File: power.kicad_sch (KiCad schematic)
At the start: 47 parts, among them J5 Ride Through, Q3 2N7002, U2 MAX17614, U3 TVS3300DRV, U4 LM61480

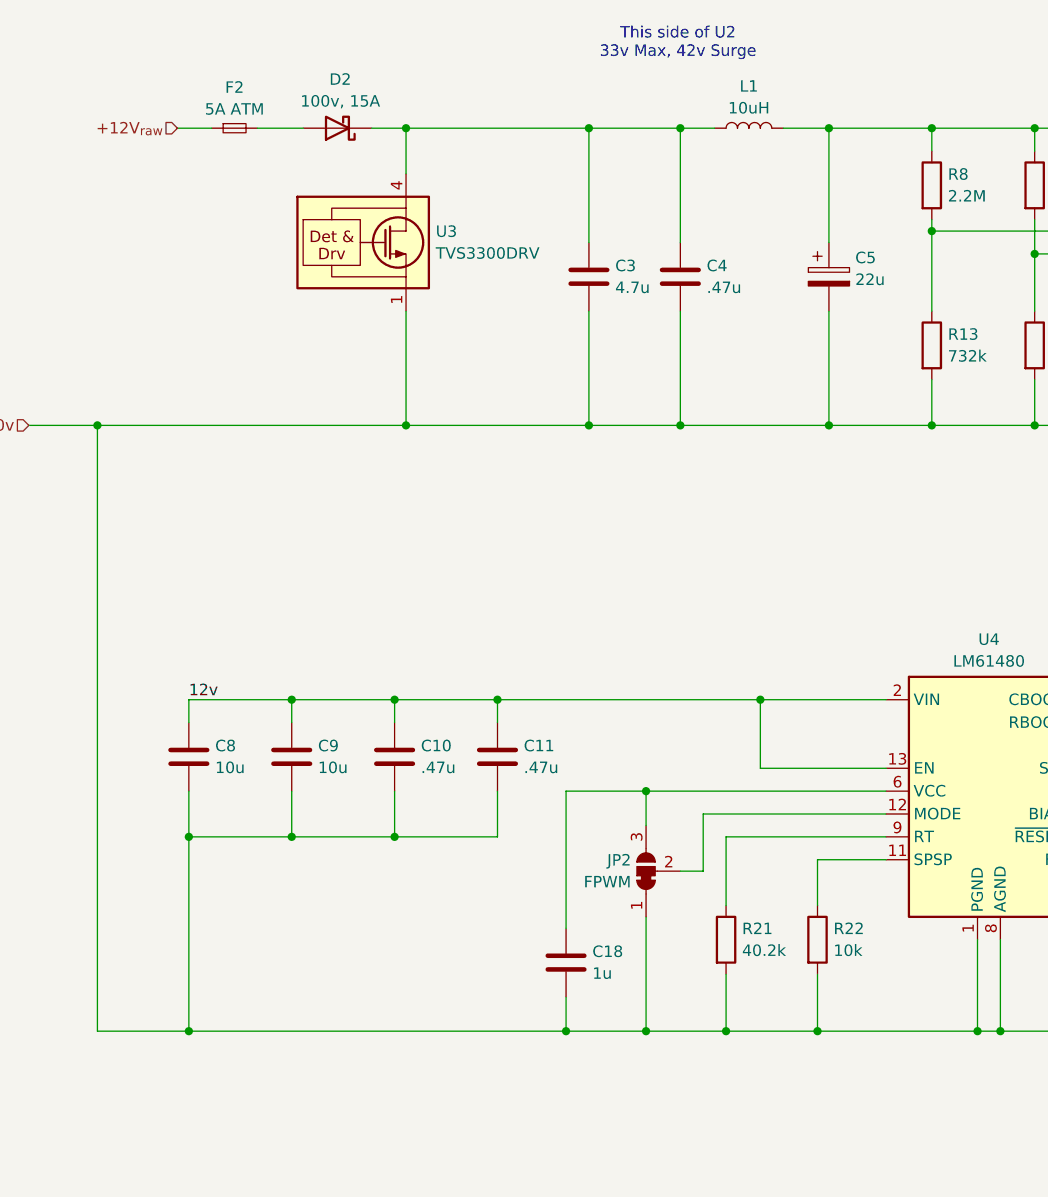
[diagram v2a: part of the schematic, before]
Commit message: second pass at layout complete
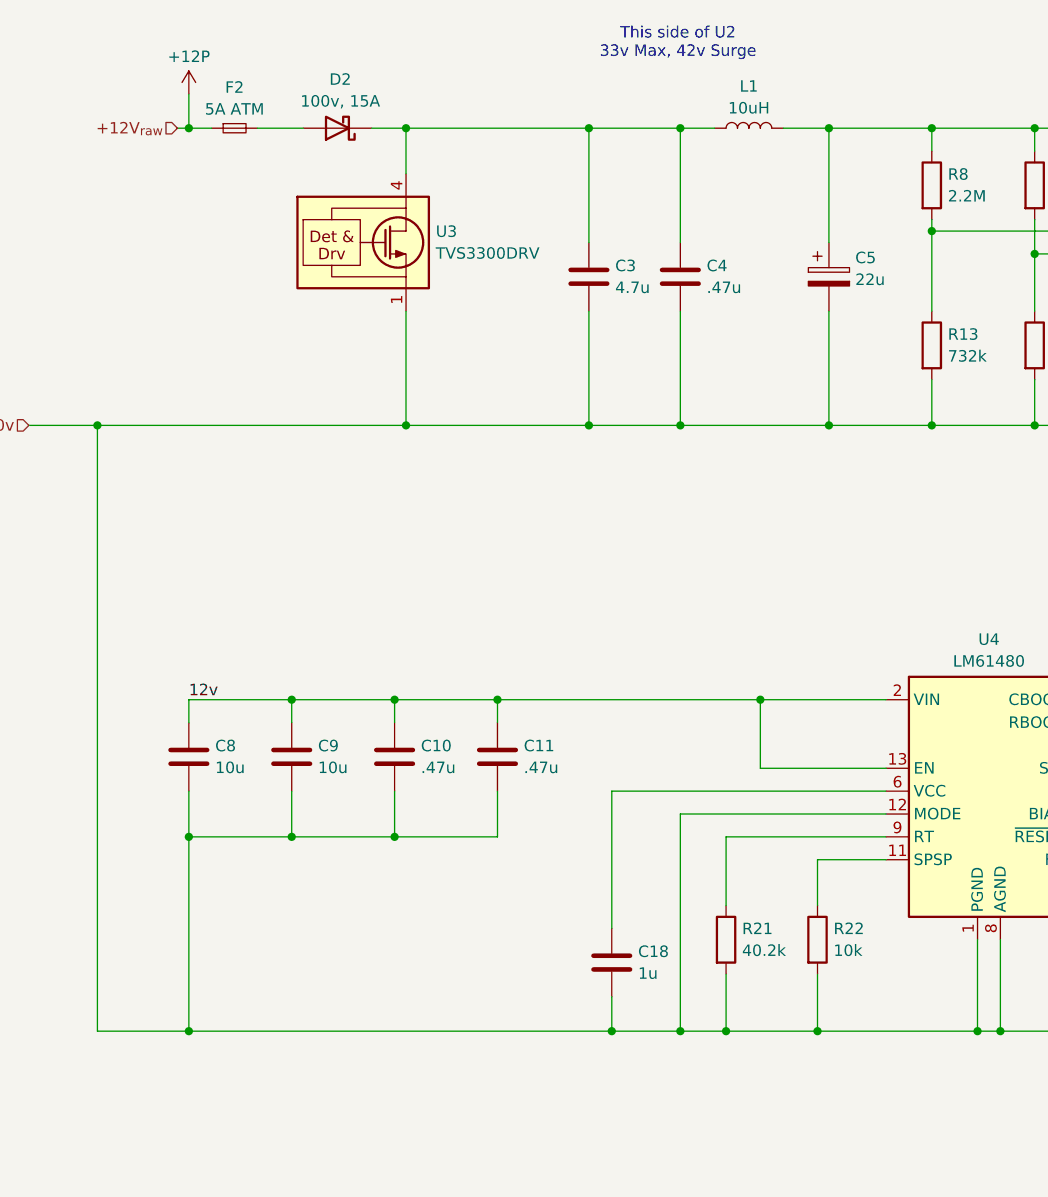
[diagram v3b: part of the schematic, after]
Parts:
- removed JP2: FPWM, Jumper:SolderJumper-3_P1.3mm_Bridged2Bar12_RoundedPad1.0x1.5mm, symbol Jumper:SolderJumper_3_Bridged12
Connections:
- net PGND: now also U4.12 (MODE)
- net +12V_{raw} renamed +12P
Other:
- moved on the sheet: C18
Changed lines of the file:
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@@
 	)
 	(junction
+		(at 85.09 133.35)
+		(diameter 0)
+		(color 0 0 0 0)
+	)
+	(junction
 		(at 260.35 33.02)
 		(diameter 0)
@@
 	)
 	(junction
+		(at 92.71 133.35)
+		(diameter 0)
+		(color 0 0 0 0)
+	)
+	(junction
 		(at 101.6 96.52)
 		(diameter 0)
@@
 	)
 	(junction
+		(at 38.1 33.02)
+		(diameter 0)
+		(color 0 0 0 0)
+	)
+	(junction
 		(at 60.96 111.76)
 		(diameter 0)
@@
 	)
 	(junction
-		(at 88.9 106.68)
-		(diameter 0)
-		(color 0 0 0 0)
-	)
-	(junction
 		(at 132.08 33.02)
 		(diameter 0)
@@
 	)
 	(junction
-		(at 88.9 133.35)
-		(diameter 0)
-		(color 0 0 0 0)
-	)
-	(junction
 		(at 227.33 33.02)
 		(diameter 0)
@@
 	)
 	(junction
-		(at 80.01 133.35)
-		(diameter 0)
-		(color 0 0 0 0)
-	)
-	(junction
 		(at 38.1 111.76)
 		(diameter 0)
@@
 	(wire
 		(pts
-			(xy 80.01 133.35) (xy 88.9 133.35)
-		)
-		(stroke
-			(width 0)
-			(type default)
-		)
-	)
-	(wire
-		(pts
 			(xy 154.94 104.14) (xy 157.48 104.14)
 		)
@@
 	(wire
 		(pts
-			(xy 38.1 133.35) (xy 80.01 133.35)
+			(xy 38.1 133.35) (xy 85.09 133.35)
 		)
 		(stroke
@@
 	(wire
 		(pts
-			(xy 88.9 133.35) (xy 97.79 133.35)
-		)
-		(stroke
-			(width 0)
-			(type default)
-		)
-	)
-	(wire
-		(pts
 			(xy 207.01 133.35) (xy 217.17 133.35)
 		)
@@
 	(wire
 		(pts
+			(xy 92.71 109.22) (xy 92.71 133.35)
+		)
+		(stroke
+			(width 0)
+			(type default)
+		)
+	)
+	(wire
+		(pts
 			(xy 184.15 157.48) (xy 184.15 160.02)
 		)
@@
 	(wire
 		(pts
-			(xy 88.9 106.68) (xy 80.01 106.68)
+			(xy 85.09 106.68) (xy 115.57 106.68)
 		)
 		(stroke
@@
 	(wire
 		(pts
-			(xy 92.71 115.57) (xy 95.25 115.57)
+			(xy 38.1 33.02) (xy 40.64 33.02)
 		)
 		(stroke
@@
 	(wire
 		(pts
-			(xy 80.01 106.68) (xy 80.01 121.92)
+			(xy 85.09 106.68) (xy 85.09 121.92)
 		)
 		(stroke
@@
 	(wire
 		(pts
-			(xy 88.9 106.68) (xy 115.57 106.68)
-		)
-		(stroke
-			(width 0)
-			(type default)
-		)
-	)
-	(wire
-		(pts
 			(xy 120.65 33.02) (xy 132.08 33.02)
 		)
@@
 	(wire
 		(pts
-			(xy 88.9 120.65) (xy 88.9 133.35)
-		)
-		(stroke
-			(width 0)
-			(type default)
-		)
-	)
-	(wire
-		(pts
 			(xy 27.94 66.04) (xy 62.23 66.04)
 		)
@@
 	(wire
 		(pts
-			(xy 36.83 33.02) (xy 40.64 33.02)
+			(xy 36.83 33.02) (xy 38.1 33.02)
 		)
 		(stroke
@@
 	(wire
 		(pts
-			(xy 80.01 129.54) (xy 80.01 133.35)
+			(xy 85.09 129.54) (xy 85.09 133.35)
 		)
 		(stroke
@@
 	(wire
 		(pts
+			(xy 38.1 29.21) (xy 38.1 33.02)
+		)
+		(stroke
+			(width 0)
+			(type default)
+		)
+	)
+	(wire
+		(pts
 			(xy 229.87 104.14) (xy 217.17 104.14)
 		)
@@
 	(wire
 		(pts
-			(xy 95.25 109.22) (xy 115.57 109.22)
+			(xy 85.09 133.35) (xy 92.71 133.35)
+		)
+		(stroke
+			(width 0)
+			(type default)
+		)
+	)
+	(wire
+		(pts
+			(xy 92.71 109.22) (xy 115.57 109.22)
 		)
 		(stroke
@@
 	(wire
 		(pts
-			(xy 125.73 133.35) (xy 128.27 133.35)
+			(xy 92.71 133.35) (xy 97.79 133.35)
 		)
 		(stroke
@@
 	(wire
 		(pts
-			(xy 45.72 33.02) (xy 50.8 33.02)
+			(xy 125.73 133.35) (xy 128.27 133.35)
 		)
 		(stroke
@@
 	(wire
 		(pts
-			(xy 88.9 106.68) (xy 88.9 110.49)
+			(xy 45.72 33.02) (xy 50.8 33.02)
 		)
 		(stroke
@@
 	(wire
 		(pts
-			(xy 95.25 115.57) (xy 95.25 109.22)
-		)
-		(stroke
-			(width 0)
-			(type default)
-		)
-	)
-	(wire
-		(pts
 			(xy 107.95 133.35) (xy 125.73 133.35)
 		)
@@
 	(symbol
 		(lib_id "Device:C")
-		(at 80.01 125.73 0)
+		(at 85.09 125.73 0)
 		(unit 1)
 		(exclude_from_sim no)
@@
 		(fields_autoplaced yes)
 		(property "Reference" "C18"
-			(at 82.931 124.5178 0)
+			(at 88.011 124.5178 0)
 			(effects
 				(font
@@
 		)
 		(property "Value" "1u"
-			(at 82.931 126.9421 0)
+			(at 88.011 126.9421 0)
 			(effects
 				(font
@@
 		)
 		(property "Footprint" "Capacitor_SMD:C_0603_1608Metric"
-			(at 80.9752 129.54 0)
+			(at 86.0552 129.54 0)
 			(effects
 				(font
@@
 		)
 		(property "Datasheet" "~"
-			(at 80.01 125.73 0)
+			(at 85.09 125.73 0)
 			(effects
 				(font
@@
 		)
 		(property "Description" "Unpolarized capacitor"
-			(at 80.01 125.73 0)
+			(at 85.09 125.73 0)
 			(effects
 				(font
@@
 		)
 		(property "Mfg Part Number" "MSAST168SB7105KTNA01"
-			(at 80.01 125.73 0)
+			(at 85.09 125.73 0)
 			(effects
 				(font
@@
 	)
 	(symbol
-		(lib_id "Jumper:SolderJumper_3_Bridged12")
-		(at 88.9 115.57 90)
-		(unit 1)
-		(exclude_from_sim yes)
-		(in_bom no)
-		(on_board yes)
-		(dnp no)
-		(fields_autoplaced yes)
-		(property "Reference" "JP2"
-			(at 87.2491 114.3578 90)
-			(effects
-				(font
-					(size 1.27 1.27)
-				)
-				(justify left)
-			)
-		)
-		(property "Value" "FPWM"
-			(at 87.2491 116.7821 90)
-			(effects
-				(font
-					(size 1.27 1.27)
-				)
-				(justify left)
-			)
-		)
-		(property "Footprint" "Jumper:SolderJumper-3_P1.3mm_Bridged2Bar12_RoundedPad1.0x1.5mm"
-			(at 88.9 115.57 0)
-			(effects
-				(font
-					(size 1.27 1.27)
-				)
-				(hide yes)
-			)
-		)
-		(property "Datasheet" "~"
-			(at 88.9 115.57 0)
-			(effects
-				(font
-					(size 1.27 1.27)
-				)
-				(hide yes)
-			)
-		)
-		(property "Description" "3-pole Solder Jumper, pins 1+2 closed/bridged"
-			(at 88.9 115.57 0)
-			(effects
-				(font
-					(size 1.27 1.27)
-				)
-				(hide yes)
-			)
-		)
-		(property "Mfg Part Number" "--"
-			(at 88.9 115.57 0)
-			(effects
-				(font
-					(size 1.27 1.27)
-				)
-				(hide yes)
-			)
-		)
-		(pin "2"
-		)
-		(pin "3"
-		)
-		(pin "1"
-		)
-		(instances
-			(project "dashHat"
-				(path "/e63e39d7-6ac0-4ffd-8aa3-1841a4541b55/c83fc454-3a65-469f-ae3e-cbb574f94c8f"
-					(reference "JP2")
-					(unit 1)
-				)
-			)
-		)
-	)
-	(symbol
 		(lib_id "Device:C")
 		(at 252.73 114.3 0)
@@
 					(unit 1)
 				)
+			)
+		)
+	)
+	(symbol
+		(lib_id "power:+12P")
+		(at 38.1 29.21 0)
+		(unit 1)
+		(exclude_from_sim no)
+		(in_bom yes)
+		(on_board yes)
+		(dnp no)
+		(fields_autoplaced yes)
+		(property "Reference" "#PWR059"
+			(at 38.1 33.02 0)
+			(effects
+				(font
+					(size 1.27 1.27)
+				)
+				(hide yes)
+			)
+		)
+		(property "Value" "+12P"
+			(at 38.1 25.0769 0)
+			(effects
+				(font
+					(size 1.27 1.27)
+				)
+			)
+		)
+		(property "Footprint" ""
+			(at 38.1 29.21 0)
+			(effects
+				(font
+					(size 1.27 1.27)
+				)
+				(hide yes)
+			)
+		)
+		(property "Datasheet" ""
+			(at 38.1 29.21 0)
+			(effects
+				(font
+					(size 1.27 1.27)
+				)
+				(hide yes)
+			)
+		)
+		(property "Description" "Power symbol creates a global label with name \"+12P\""
+			(at 38.1 29.21 0)
+			(effects
+				(font
+					(size 1.27 1.27)
+				)
+				(hide yes)
+			)
+		)
+		(pin "1"
+		)
+		(instances
+			(project "dashHat"
+				(path "/e63e39d7-6ac0-4ffd-8aa3-1841a4541b55/c83fc454-3a65-469f-ae3e-cbb574f94c8f"
+					(reference "#PWR059")
+					(unit 1)
+				)

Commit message: filled in mfg part number for ordering
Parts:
- J5: Mfg Part Number (none) -> --
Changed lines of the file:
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@@
+			)
+		)
+		(property "Mfg Part Number" "--"
+			(at 266.7 63.5 0)
+			(effects
+				(font
+					(size 1.27 1.27)
+				)
+				(hide yes)
 			)
 		)

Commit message: bug fixes from testing
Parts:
- L2: footprint Inductor_SMD:L_Coilcraft_XAL7030-272 -> Custom:L_Coilcraft_XAL7030-272
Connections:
- net +12P: now also C3.1, C4.1, D2.1 (K), F2.2, L1.1, U3.4 (IN), U3.5 (IN), U3.6 (IN); no longer F2.1
- net PGND: now also D2.2 (A)
- net at R14.1, R9.2: now also U2.5 (OVLO); no longer U2.4 (UVLO)
- net at R13.1, R8.2: now also U2.4 (UVLO); no longer U2.5 (OVLO)
- new net +12v_raw: F2.1
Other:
- moved on the sheet: D2, R13, R14, R8, R9, U3

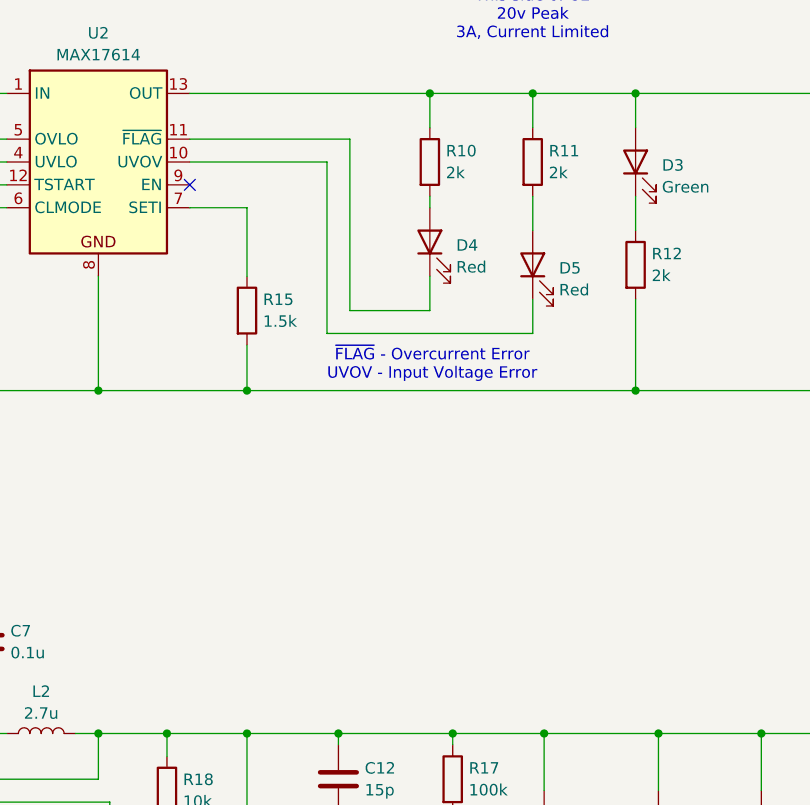
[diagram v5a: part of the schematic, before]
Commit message: added a switch to the lcd, and feedback from the 12v input to the pi
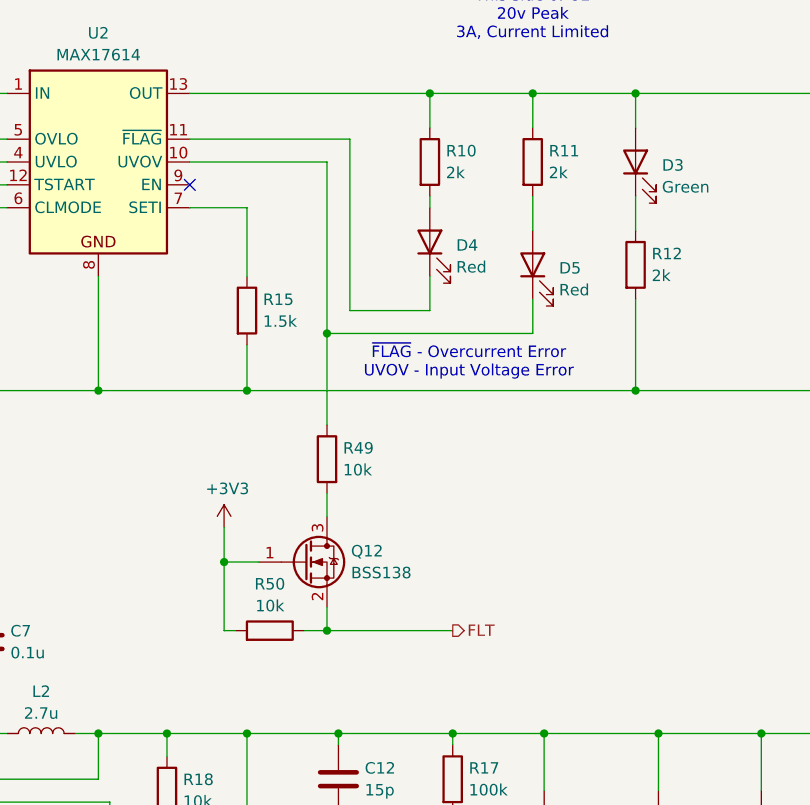
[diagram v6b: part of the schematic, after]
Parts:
- added Q12: BSS138, Package_TO_SOT_SMD:SOT-23, symbol Transistor_FET:BSS138
- added R49, R50: 10k, Resistor_SMD:R_0603_1608Metric, symbol Device:R
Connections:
- net at D5.1 (K), U2.10 (UVOV): now also R49.1
- new net: Q12.3 (D), R49.2
- new net +3V3: Q12.1 (G), R50.2
- new net FLT: Q12.2 (S), R50.1

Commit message: selectable current limit mode
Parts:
- added R48: 0, Resistor_SMD:R_0603_1608Metric, symbol Device:R
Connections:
- net PGND: now also R48.2; no longer U2.6 (CLMODE)
- new net: R48.1, U2.6 (CLMODE)

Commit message: update resistors to more commmon values
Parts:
- R19: value 560 -> 680
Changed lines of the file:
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@@
 			)
 		)
-		(property "Value" "560"
+		(property "Value" "680"
 			(at 185.928 120.5921 0)
 			(effects
